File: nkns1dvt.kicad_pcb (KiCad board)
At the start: 2 copper layers, 168.9 x 126.5 mm, 77 parts, among them J1 MJ-4PP-9, J2 SERIAL_LED, SW1 SW_RESET, SW10 SW_PUSH, SW11 SW_PUSH, SW12 SW_PUSH, SW13 SW_PUSH, SW14 SW_PUSH, SW15 SW_PUSH, SW16 SW_PUSH, SW17 SW_PUSH, SW18 SW_PUSH, SW19 SW_PUSH, SW2 SW_PUSH, SW20 SW_PUSH, SW21 SW_PUSH, SW22 SW_PUSH, SW23 SW_PUSH, SW24 SW_PUSH, SW25 SW_PUSH, SW26 SW_PUSH, SW27 SW_PUSH, SW28 SW_PUSH, SW29 SW_PUSH, SW3 SW_PUSH, SW30 SW_PUSH, SW31 SW_PUSH, SW32 SW_PUSH, SW33 SW_PUSH, SW34 SW_PUSH, SW4 SW_PUSH, SW5 SW_PUSH, SW6 SW_PUSH, SW7 SW_PUSH, SW8 SW_PUSH, SW9 SW_PUSH, U1 ProMicro

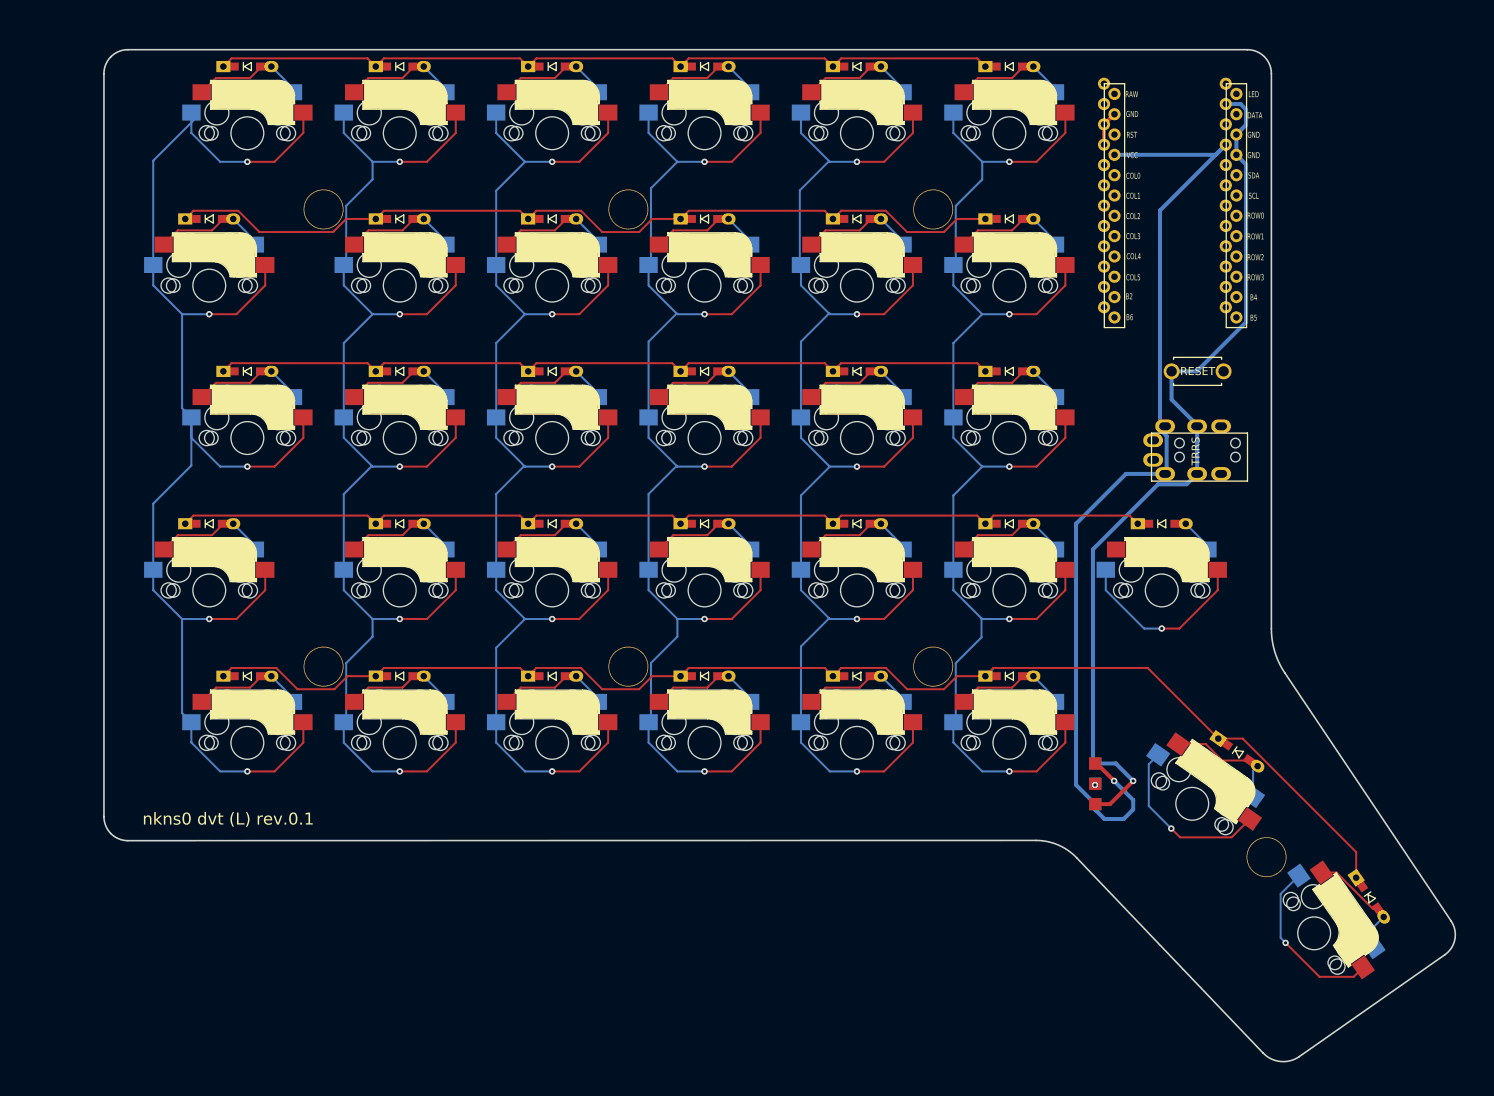
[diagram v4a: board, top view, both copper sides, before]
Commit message: Add wire. Add Mounting hole for ProMicro Area Plate.
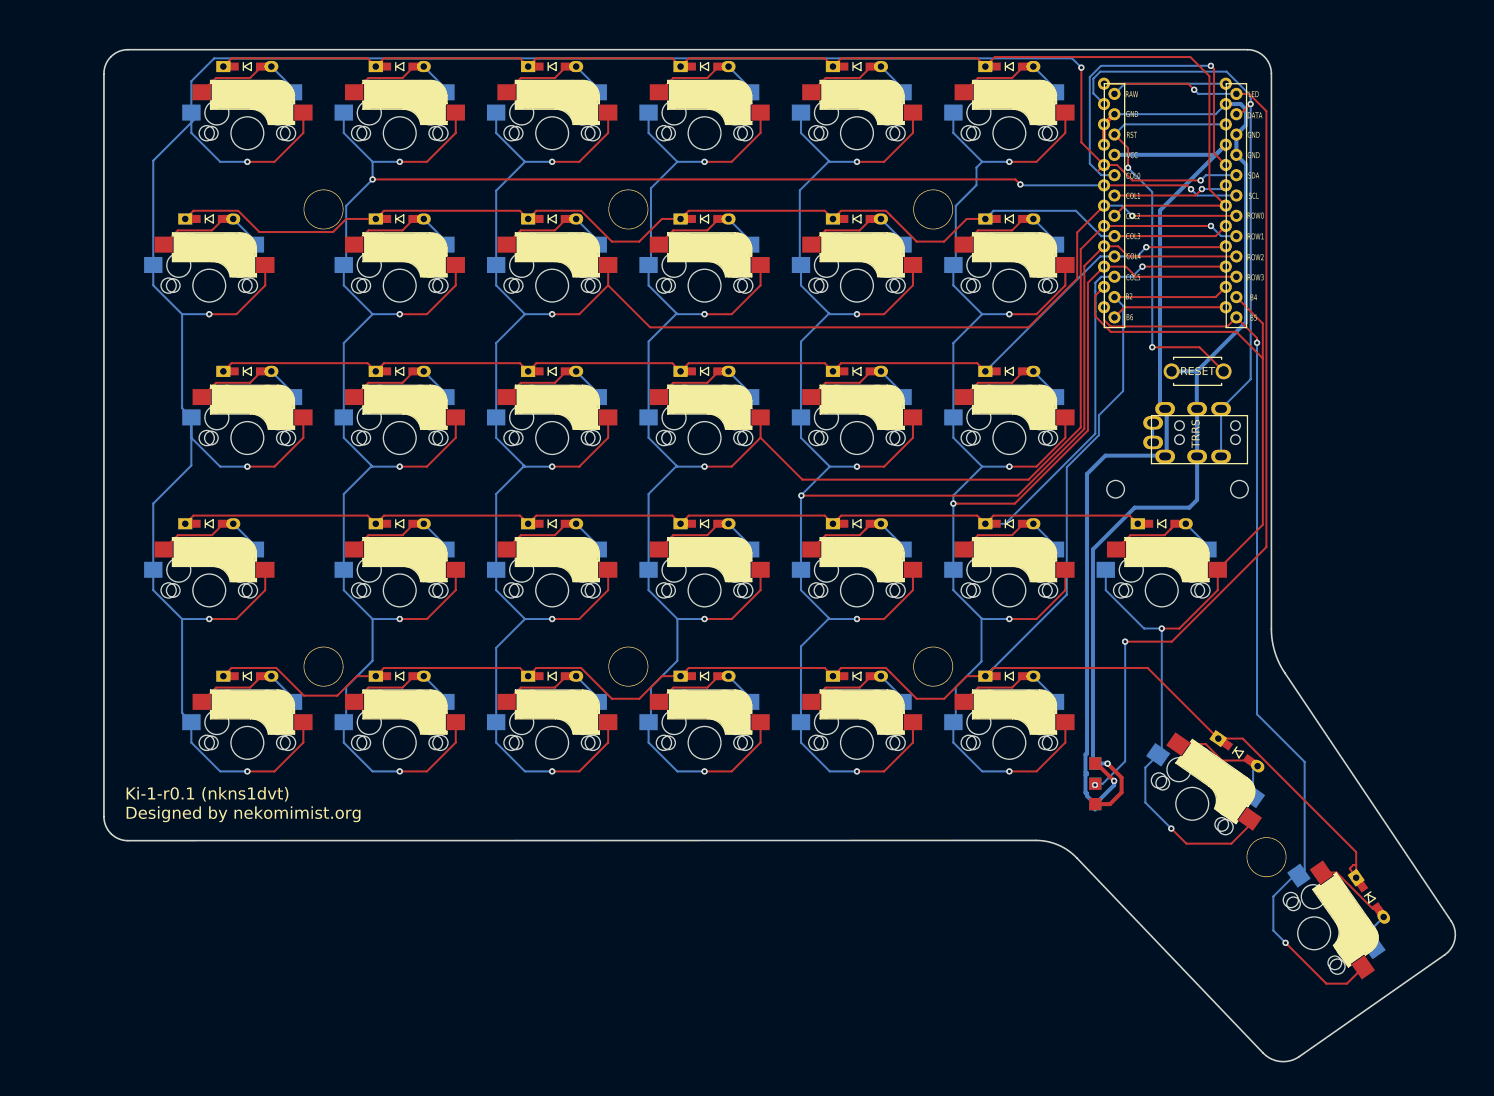
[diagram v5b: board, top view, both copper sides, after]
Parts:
- added Hole1: Hole M2, MountingHole:MountingHole_2.2mm_M2, F.Cu at (154.8, 76.2)
- added Hole2: Hole M2, MountingHole:MountingHole_2.2mm_M2, F.Cu at (170.3, 76.2)
- moved J1 2.18 mm to (171.3, 70.0)
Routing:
- net col0: track 180.0 -> 328.9 mm, vias 5 -> 7
- net led: track 0.03 -> 120.5 mm, vias 1 -> 3
- net col1: track 167.9 -> 276.9 mm, vias 5 -> 8
- net col7: track 21.6 -> 117.3 mm, vias 1 -> 2
- net col2: track 167.9 -> 259.4 mm, vias 5 -> 6
- net col3: track 168.5 -> 256.9 mm, vias 5 -> 6
- net col6: track 45.2 -> 127.6 mm
- net row4: track 165.7 -> 247.2 mm
- net col4: track 168.2 -> 248.0 mm, vias 5 -> 6
- net data: track 0.00 -> 73.9 mm, vias 0 -> 1
- net row0: track 99.5 -> 166.0 mm
- net row3: track 124.1 -> 185.3 mm, vias 0 -> 1
- net col5: track 168.0 -> 227.0 mm, vias 5 -> 6
- net reset: track 0.00 -> 53.2 mm, vias 0 -> 2
- net Net-(U1-Pad20): track 0.00 -> 43.4 mm, vias 0 -> 1
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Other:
- board text added: "Ki-1-r0.1 (nkns1dvt) Designed by nekomimist.org"
- board text removed: "nkns0 dvt (L) rev.0.1"

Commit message: Add beta-GND
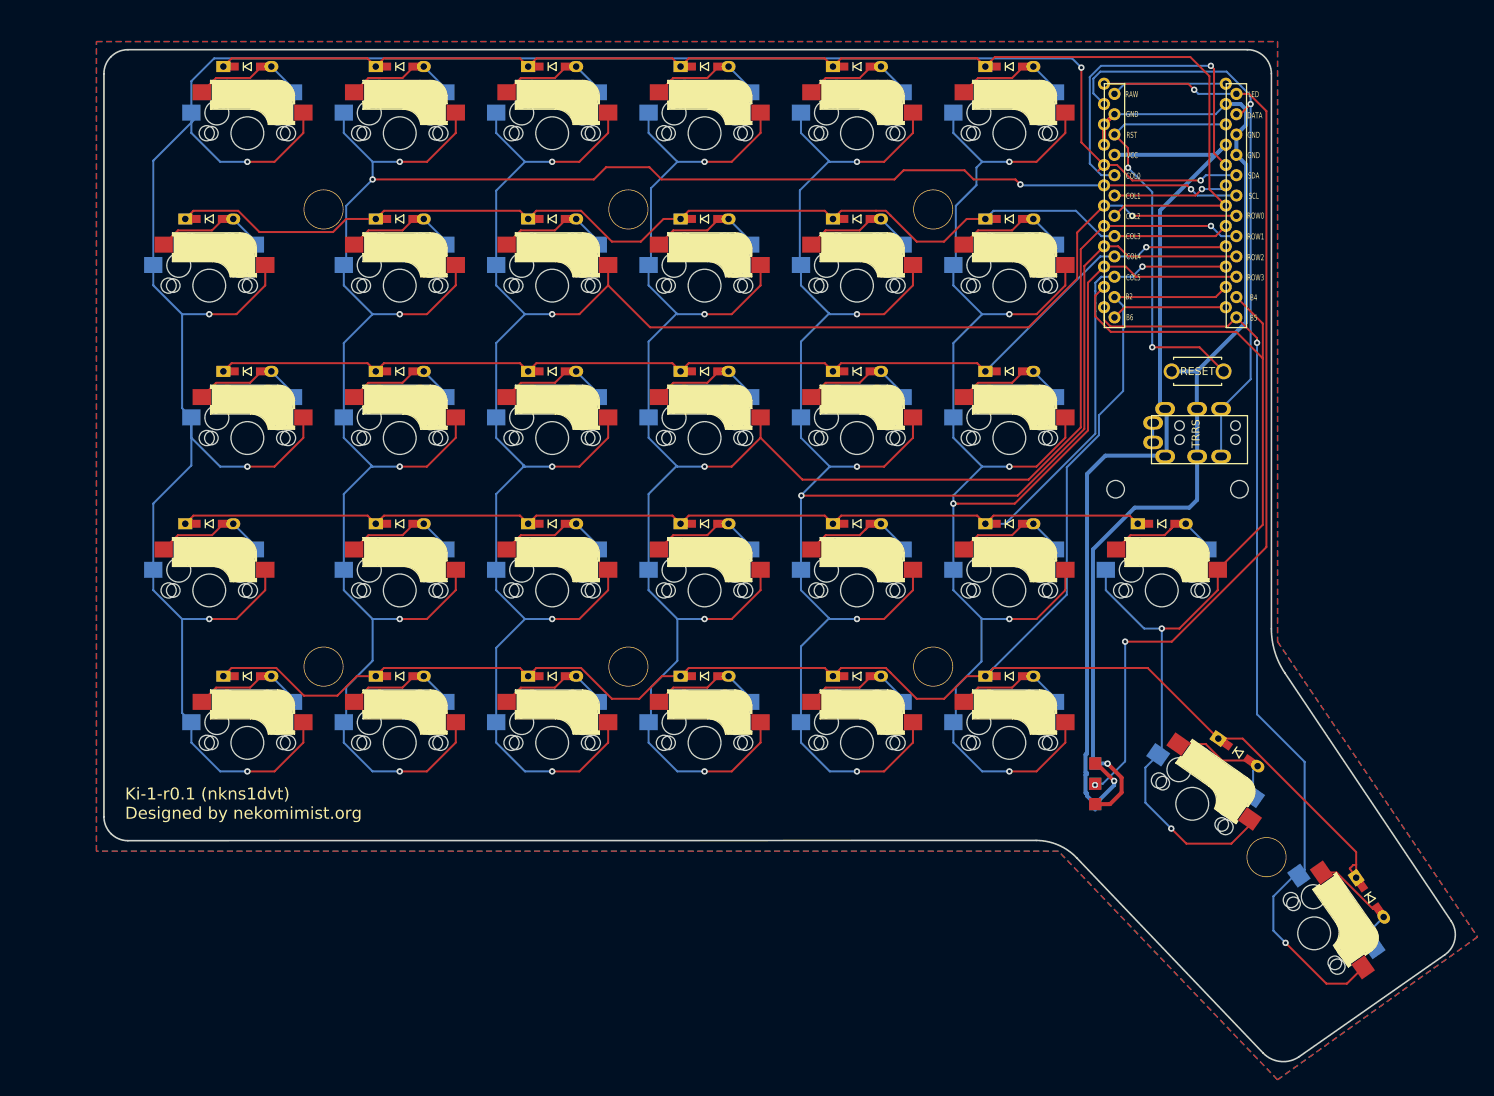
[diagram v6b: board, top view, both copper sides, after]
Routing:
- net col1: track 276.9 -> 279.1 mm
- added copper zone on B.Cu, net GND
- added copper zone on F.Cu, net GND

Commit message: Update
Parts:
- moved Hole4 9.82 mm to (53.4, 88.8)
- moved Hole1 9.82 mm to (53.4, 50.8)
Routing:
- net col1: track 279.1 -> 276.9 mm
- net row4: track 247.2 -> 245.2 mm
- net row1: track 148.5 -> 147.1 mm
- removed copper zone on B.Cu, net GND
- removed copper zone on F.Cu, net GND

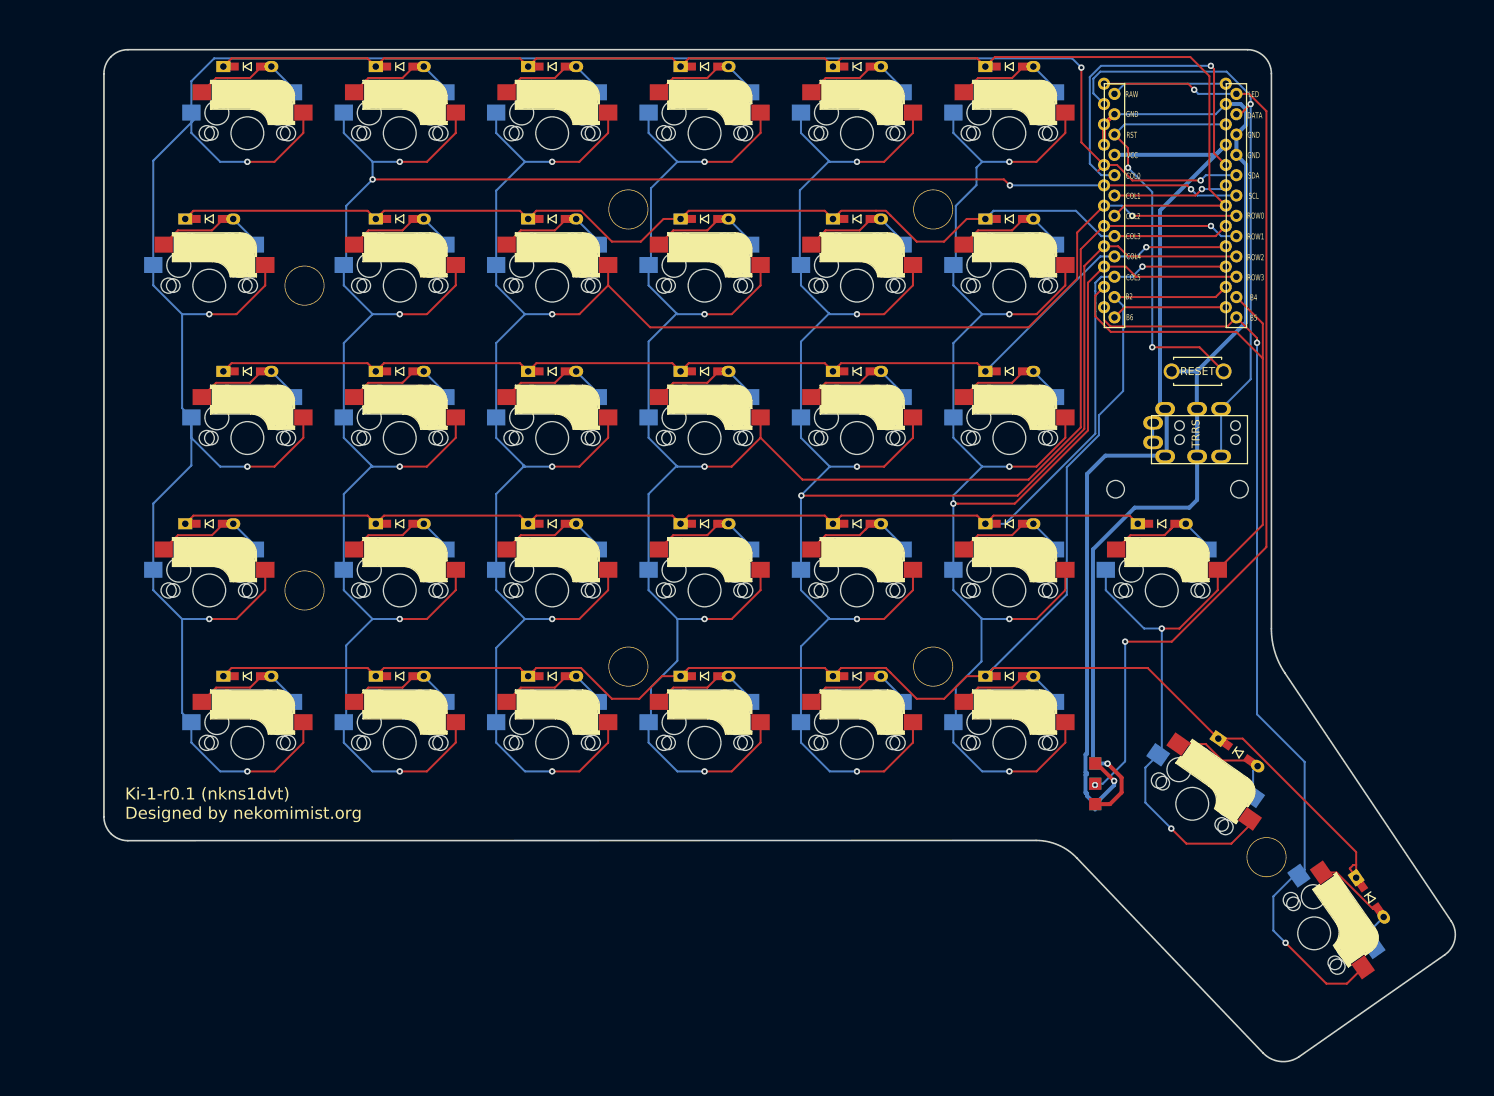
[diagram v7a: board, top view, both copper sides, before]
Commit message: Change diode footprints
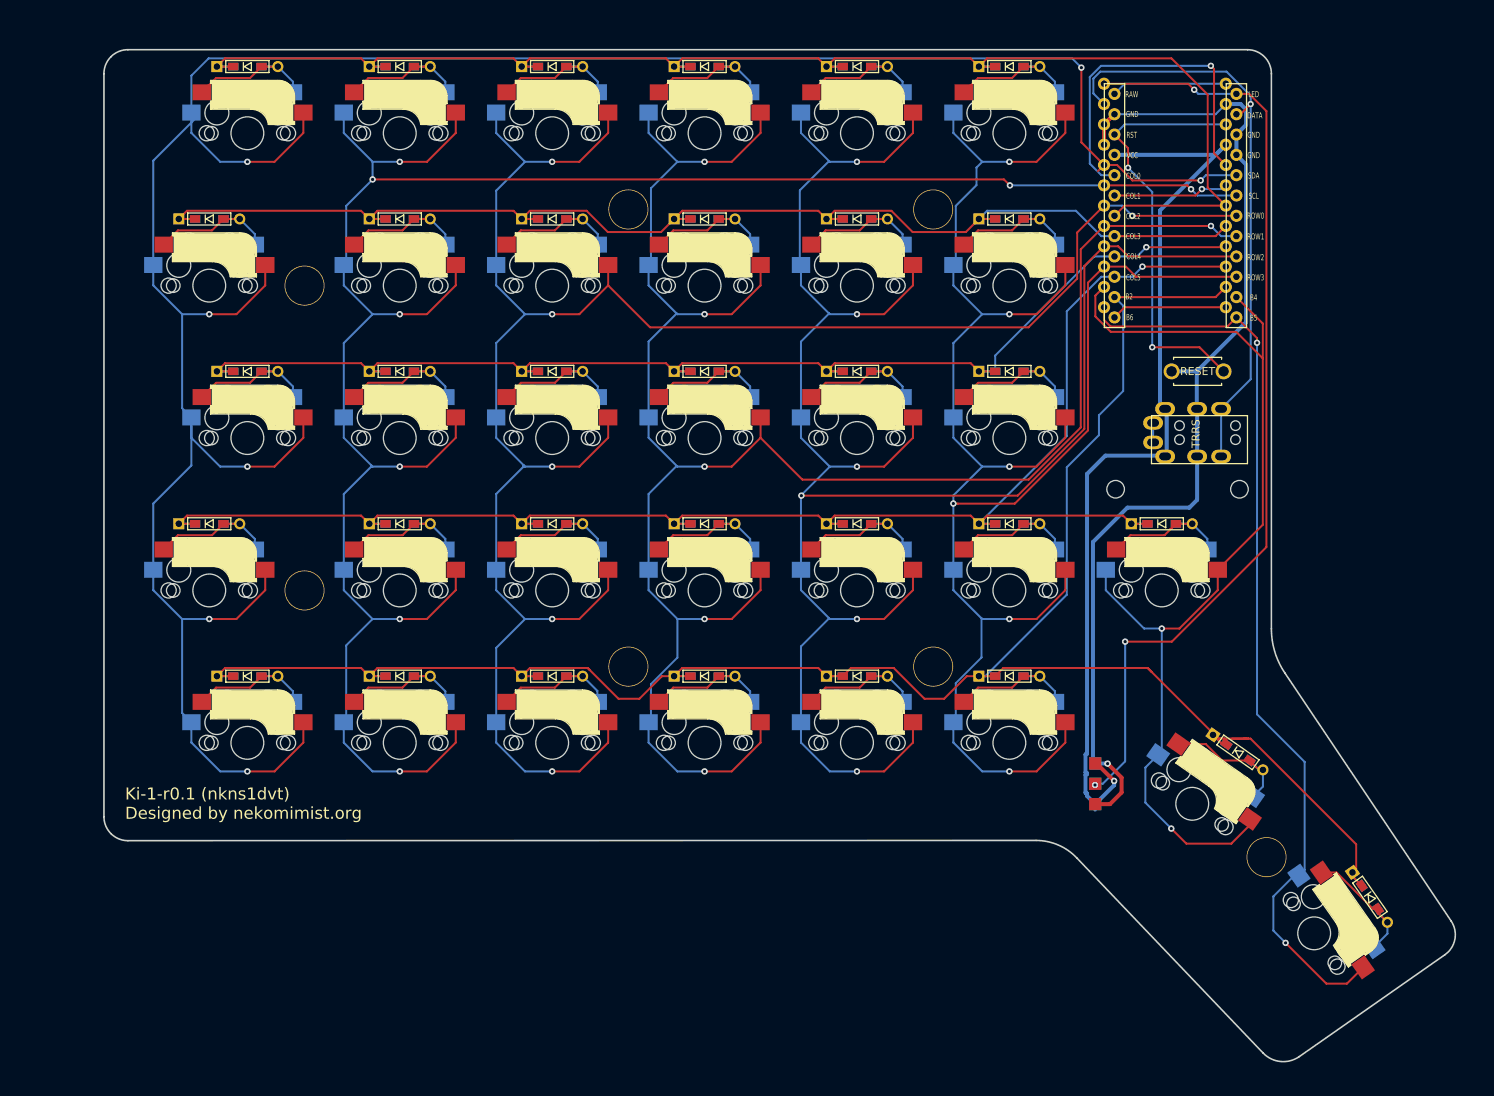
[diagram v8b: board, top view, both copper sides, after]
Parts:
- D1, D10, D11, D12, D13, D14, D15, D16, D17, D18, D19, D2, D20, D21, D22, D23, D24, D25, D26, D27, D28, D29, D3, D30, D31, D32, D33, D4, D5, D6, D7, D8, D9: footprint kbd:D3_TH -> kbd:D3_TH_SMD
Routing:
- net row4: track 245.2 -> 268.6 mm
- net row3: track 185.3 -> 206.7 mm
- net row2: track 141.9 -> 160.4 mm
- net row0: track 166.0 -> 184.1 mm
- net row1: track 147.1 -> 164.5 mm
- net Net-(D32-Pad2): track 16.1 -> 20.0 mm
- net Net-(D33-Pad2): track 15.5 -> 19.2 mm
- net Net-(D25-Pad2): track 15.4 -> 18.4 mm
- net Net-(D23-Pad2): track 15.4 -> 18.4 mm
- net Net-(D9-Pad2): track 14.4 -> 17.4 mm
- net Net-(D15-Pad2): track 14.4 -> 17.4 mm
- net Net-(D21-Pad2): track 14.4 -> 17.4 mm
- net Net-(D3-Pad2): track 14.4 -> 17.4 mm
- net Net-(D14-Pad2): track 14.4 -> 17.4 mm
- net Net-(D20-Pad2): track 14.4 -> 17.4 mm
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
